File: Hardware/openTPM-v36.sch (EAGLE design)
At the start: 69 parts, among them U1 SAM4S4A, U2 TPS62172, U3 TC58CVG0S3HQAIEWSON, Y1 12MHZ, Y2 32KHz

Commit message: v36
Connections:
- new net N$19: U1.PA9/PGMM1, U3.CS
- new net N$24: U1.PA5/PGMRDY, U3.HOLD/SO3
- new net N$25: U1.PA6/PGMNOE, U3.WP/SO2
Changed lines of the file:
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@@
 <?xml version="1.0" encoding="utf-8"?>
 <!DOCTYPE eagle SYSTEM "eagle.dtd">
-<eagle version="8.1.1">
+<eagle version="7.4.0">
 <drawing>
 <settings>
@@
 <instance part="JP1" gate="G$1" x="45.72" y="116.84" rot="R180"/>
 <instance part="TPM1" gate="G$1" x="246.38" y="154.94"/>
-<instance part="GND1" gate="1" x="226.06" y="114.3"/>
-<instance part="GND2" gate="1" x="279.4" y="114.3"/>
+<instance part="GND1" gate="1" x="226.06" y="104.14"/>
+<instance part="GND2" gate="1" x="279.4" y="104.14"/>
 <instance part="GND3" gate="1" x="55.88" y="101.6"/>
 <instance part="GND5" gate="1" x="154.94" y="96.52"/>
@@
 <pinref part="GND2" gate="1" pin="GND"/>
 <wire x1="264.16" y1="142.24" x2="279.4" y2="142.24" width="0.1524" layer="91"/>
-<wire x1="279.4" y1="142.24" x2="279.4" y2="116.84" width="0.1524" layer="91"/>
+<wire x1="279.4" y1="142.24" x2="279.4" y2="106.68" width="0.1524" layer="91"/>
 <pinref part="TPM1" gate="G$1" pin="GND@25"/>
 <wire x1="264.16" y1="167.64" x2="279.4" y2="167.64" width="0.1524" layer="91"/>
@@
 <pinref part="TPM1" gate="G$1" pin="TESTBI"/>
 <wire x1="226.06" y1="134.62" x2="226.06" y2="132.08" width="0.1524" layer="91"/>
-<wire x1="226.06" y1="132.08" x2="226.06" y2="116.84" width="0.1524" layer="91"/>
+<wire x1="226.06" y1="132.08" x2="226.06" y2="106.68" width="0.1524" layer="91"/>
 <wire x1="231.14" y1="149.86" x2="226.06" y2="149.86" width="0.1524" layer="91"/>
 <wire x1="226.06" y1="149.86" x2="226.06" y2="142.24" width="0.1524" layer="91"/>
@@
 </segment>
 </net>
+<net name="N$19" class="0">
+<segment>
+<pinref part="U1" gate="G$1" pin="PA9/PGMM1"/>
+<wire x1="152.4" y1="149.86" x2="175.26" y2="149.86" width="0.1524" layer="91"/>
+<wire x1="175.26" y1="149.86" x2="175.26" y2="116.84" width="0.1524" layer="91"/>
+<wire x1="175.26" y1="116.84" x2="342.9" y2="116.84" width="0.1524" layer="91"/>
+<wire x1="342.9" y1="116.84" x2="342.9" y2="246.38" width="0.1524" layer="91"/>
+<pinref part="U3" gate="G$1" pin="CS"/>
+<wire x1="342.9" y1="246.38" x2="365.76" y2="246.38" width="0.1524" layer="91"/>
+</segment>
+</net>
+<net name="N$24" class="0">
+<segment>
+<pinref part="U1" gate="G$1" pin="PA5/PGMRDY"/>
+<wire x1="152.4" y1="160.02" x2="182.88" y2="160.02" width="0.1524" layer="91"/>
+<wire x1="182.88" y1="160.02" x2="182.88" y2="111.76" width="0.1524" layer="91"/>
+<wire x1="182.88" y1="111.76" x2="355.6" y2="111.76" width="0.1524" layer="91"/>
+<wire x1="355.6" y1="111.76" x2="355.6" y2="203.2" width="0.1524" layer="91"/>
+<wire x1="355.6" y1="203.2" x2="416.56" y2="203.2" width="0.1524" layer="91"/>
+<wire x1="416.56" y1="203.2" x2="416.56" y2="236.22" width="0.1524" layer="91"/>
+<pinref part="U3" gate="G$1" pin="HOLD/SO3"/>
+<wire x1="416.56" y1="236.22" x2="396.24" y2="236.22" width="0.1524" layer="91"/>
+</segment>
+</net>
+<net name="N$25" class="0">
+<segment>
+<pinref part="U1" gate="G$1" pin="PA6/PGMNOE"/>
+<wire x1="152.4" y1="157.48" x2="180.34" y2="157.48" width="0.1524" layer="91"/>
+<wire x1="180.34" y1="157.48" x2="180.34" y2="114.3" width="0.1524" layer="91"/>
+<wire x1="180.34" y1="114.3" x2="353.06" y2="114.3" width="0.1524" layer="91"/>
+<wire x1="353.06" y1="114.3" x2="353.06" y2="231.14" width="0.1524" layer="91"/>
+<pinref part="U3" gate="G$1" pin="WP/SO2"/>
+<wire x1="353.06" y1="231.14" x2="365.76" y2="231.14" width="0.1524" layer="91"/>
+</segment>
+</net>

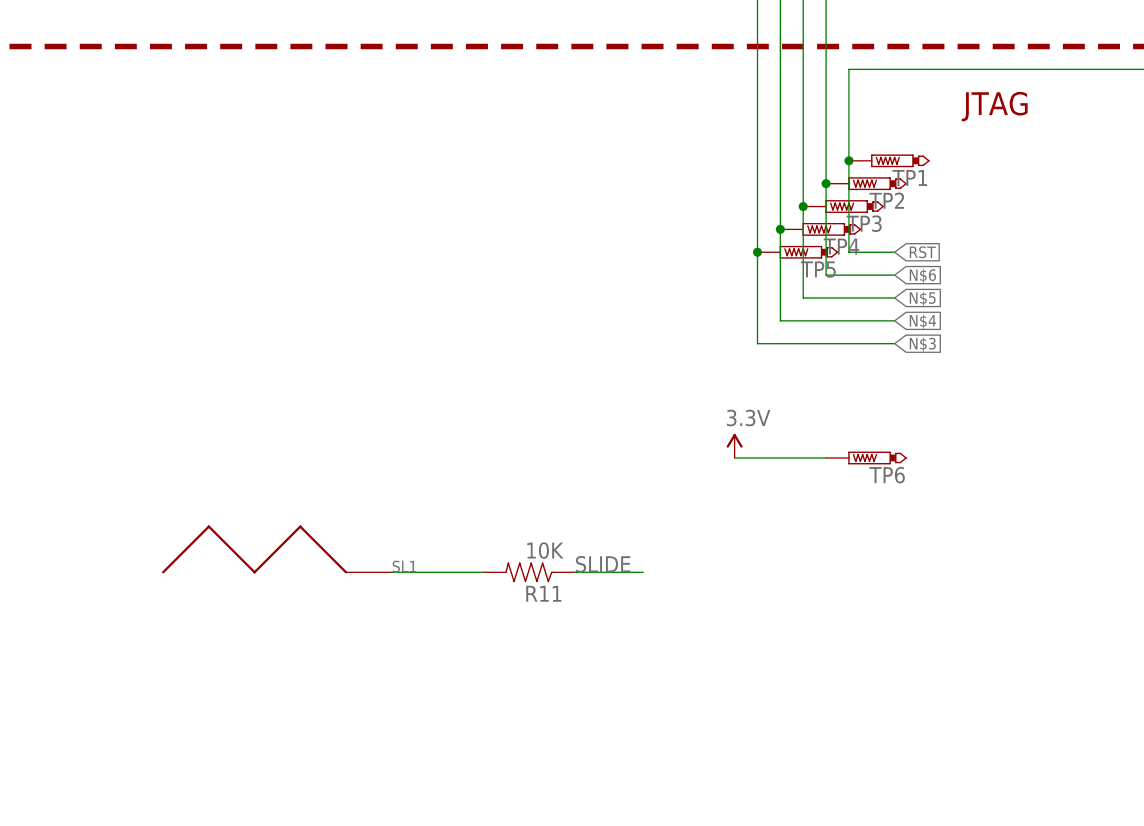
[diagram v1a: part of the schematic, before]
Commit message: cleaned silk up, added logo and binary words.
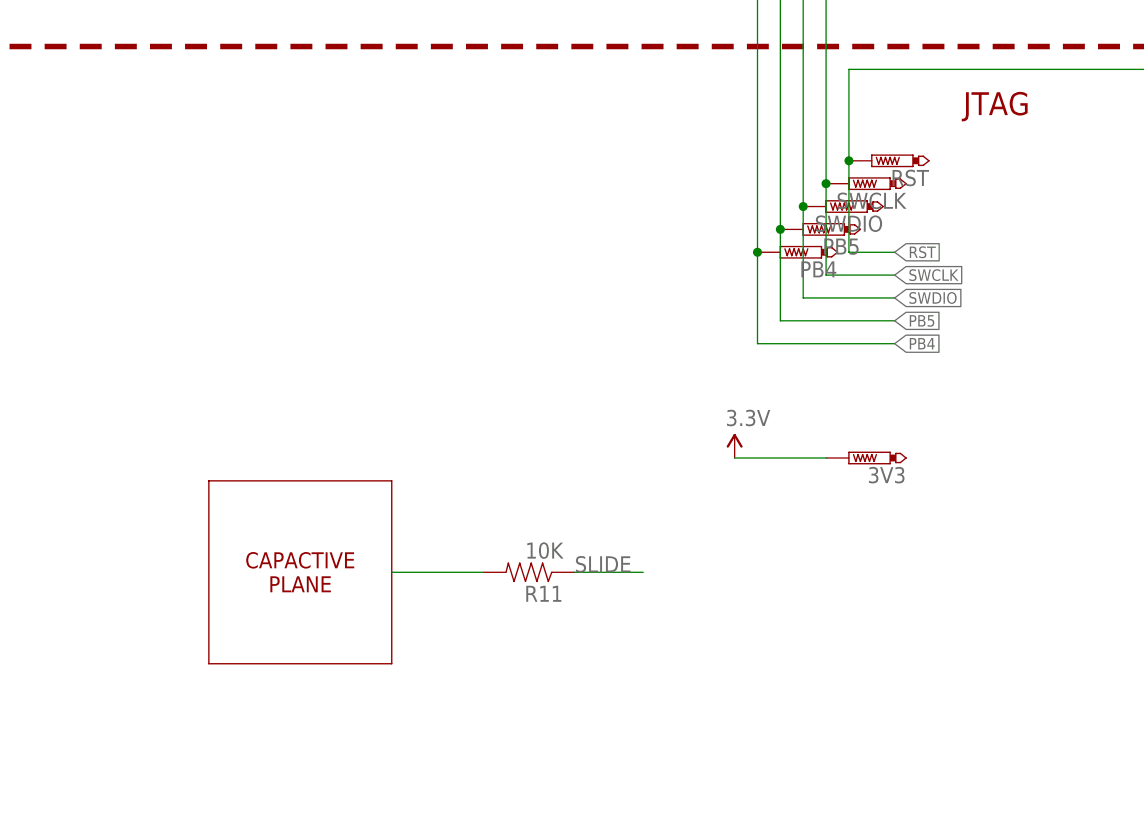
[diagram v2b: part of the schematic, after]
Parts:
- removed SL1: SLIDER_PASSIVE_1SEG, u2ftoken:SLIDER_PASSIVE_1SEG
- renumbered TP1 to RST, TP2 to SWCLK, TP3 to SWDIO, TP4 to PB5, TP5 to PB4, TP6 to 3V3
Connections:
- net N$3 renamed PB4
- net N$4 renamed PB5
- net N$5 renamed SWDIO
- net N$6 renamed SWCLK
- removed net N$7: R11.2, SL1.SL1
- new net CAP: R11.2
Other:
- note added: "CAPACTIVE PLANE"
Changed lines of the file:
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@@
 <?xml version="1.0" encoding="utf-8"?>
 <!DOCTYPE eagle SYSTEM "eagle.dtd">
-<eagle version="7.4.0">
+<eagle version="8.1.1">
 <drawing>
 <settings>
@@
 <part name="SUPPLY20" library="TPM" deviceset="3.3V" device=""/>
 <part name="GND23" library="TPM" deviceset="GND" device=""/>
-<part name="SL1" library="u2ftoken" deviceset="SLIDER_PASSIVE_1SEG" device=""/>
-<part name="TP1" library="CHEEPER-REV0.51A" deviceset="PTR1" device="B1,27"/>
-<part name="TP2" library="CHEEPER-REV0.51A" deviceset="PTR1" device="B1,27"/>
-<part name="TP3" library="CHEEPER-REV0.51A" deviceset="PTR1" device="B1,27"/>
-<part name="TP4" library="CHEEPER-REV0.51A" deviceset="PTR1" device="B1,27"/>
-<part name="TP5" library="CHEEPER-REV0.51A" deviceset="PTR1" device="B1,27"/>
+<part name="RST" library="CHEEPER-REV0.51A" deviceset="PTR1" device="B1,27"/>
+<part name="SWCLK" library="CHEEPER-REV0.51A" deviceset="PTR1" device="B1,27"/>
+<part name="SWDIO" library="CHEEPER-REV0.51A" deviceset="PTR1" device="B1,27"/>
+<part name="PB5" library="CHEEPER-REV0.51A" deviceset="PTR1" device="B1,27"/>
+<part name="PB4" library="CHEEPER-REV0.51A" deviceset="PTR1" device="B1,27"/>
 <part name="R11" library="TPM" deviceset="RESISTOR" device=".0402" value="10K"/>
-<part name="TP6" library="CHEEPER-REV0.51A" deviceset="PTR1" device="B1,27"/>
+<part name="3V3" library="CHEEPER-REV0.51A" deviceset="PTR1" device="B1,27"/>
 <part name="SUPPLY27" library="TPM" deviceset="3.3V" device=""/>
 </parts>
@@
 <text x="106.68" y="83.82" size="2.54" layer="94" font="vector" ratio="12">JTAG</text>
 <text x="363.22" y="187.96" size="2.54" layer="94" font="vector" ratio="12">Power Decoupling</text>
+<wire x1="43.18" y1="43.18" x2="22.86" y2="43.18" width="0.1524" layer="94"/>
+<wire x1="22.86" y1="43.18" x2="22.86" y2="22.86" width="0.1524" layer="94"/>
+<wire x1="22.86" y1="22.86" x2="43.18" y2="22.86" width="0.1524" layer="94"/>
+<wire x1="43.18" y1="22.86" x2="43.18" y2="43.18" width="0.1524" layer="94"/>
+<text x="33.02" y="33.02" size="1.778" layer="94" align="center">CAPACTIVE
+PLANE</text>
 </plain>
 <instances>
@@
 <instance part="SUPPLY20" gate="G$1" x="401.32" y="251.46"/>
 <instance part="GND23" gate="1" x="398.78" y="223.52"/>
-<instance part="SL1" gate="SL1" x="27.94" y="33.02"/>
-<instance part="TP1" gate="G$1" x="96.52" y="78.74" rot="R90"/>
-<instance part="TP2" gate="G$1" x="93.98" y="76.2" rot="R90"/>
-<instance part="TP3" gate="G$1" x="91.44" y="73.66" rot="R90"/>
-<instance part="TP4" gate="G$1" x="88.9" y="71.12" rot="R90"/>
-<instance part="TP5" gate="G$1" x="86.36" y="68.58" rot="R90"/>
+<instance part="RST" gate="G$1" x="96.52" y="78.74" rot="R90"/>
+<instance part="SWCLK" gate="G$1" x="93.98" y="76.2" rot="R90"/>
+<instance part="SWDIO" gate="G$1" x="91.44" y="73.66" rot="R90"/>
+<instance part="PB5" gate="G$1" x="88.9" y="71.12" rot="R90"/>
+<instance part="PB4" gate="G$1" x="86.36" y="68.58" rot="R90"/>
 <instance part="R11" gate="G$1" x="58.42" y="33.02" rot="R180"/>
-<instance part="TP6" gate="G$1" x="93.98" y="45.72" rot="R90"/>
+<instance part="3V3" gate="G$1" x="93.98" y="45.72" rot="R90"/>
 <instance part="SUPPLY27" gate="G$1" x="81.28" y="45.72"/>
 </instances>
@@
 </segment>
 </net>
-<net name="N$3" class="0">
+<net name="PB4" class="0">
 <segment>
 <pinref part="U1" gate="G$1" pin="TDI/PB4"/>
@@
 <wire x1="83.82" y1="58.42" x2="99.06" y2="58.42" width="0.1524" layer="91"/>
 <label x="99.06" y="58.42" size="1.27" layer="95" xref="yes"/>
-<pinref part="TP5" gate="G$1" pin="TP"/>
+<pinref part="PB4" gate="G$1" pin="TP"/>
 <junction x="83.82" y="68.58"/>
 </segment>
 </net>
-<net name="N$4" class="0">
+<net name="PB5" class="0">
 <segment>
 <pinref part="U1" gate="G$1" pin="TDO/TRACESWO/PB5"/>
@@
 <wire x1="86.36" y1="60.96" x2="99.06" y2="60.96" width="0.1524" layer="91"/>
 <label x="99.06" y="60.96" size="1.27" layer="95" xref="yes"/>
-<pinref part="TP4" gate="G$1" pin="TP"/>
+<pinref part="PB5" gate="G$1" pin="TP"/>
 <junction x="86.36" y="71.12"/>
 </segment>
 </net>
-<net name="N$5" class="0">
+<net name="SWDIO" class="0">
 <segment>
 <pinref part="U1" gate="G$1" pin="TMS/SWDIO/PB6"/>
@@
 <wire x1="88.9" y1="63.5" x2="99.06" y2="63.5" width="0.1524" layer="91"/>
 <label x="99.06" y="63.5" size="1.27" layer="95" xref="yes"/>
-<pinref part="TP3" gate="G$1" pin="TP"/>
+<pinref part="SWDIO" gate="G$1" pin="TP"/>
 <junction x="88.9" y="73.66"/>
 </segment>
 </net>
-<net name="N$6" class="0">
+<net name="SWCLK" class="0">
 <segment>
 <pinref part="U1" gate="G$1" pin="TCK/SWCLK/PB7"/>
@@
 <wire x1="91.44" y1="66.04" x2="99.06" y2="66.04" width="0.1524" layer="91"/>
 <label x="99.06" y="66.04" size="1.27" layer="95" xref="yes"/>
-<pinref part="TP2" gate="G$1" pin="TP"/>
+<pinref part="SWCLK" gate="G$1" pin="TP"/>
 <junction x="91.44" y="76.2"/>
 </segment>
@@
 </segment>
 <segment>
-<pinref part="TP6" gate="G$1" pin="TP"/>
+<pinref part="3V3" gate="G$1" pin="TP"/>
 <wire x1="91.44" y1="45.72" x2="81.28" y2="45.72" width="0.1524" layer="91"/>
 <pinref part="SUPPLY27" gate="G$1" pin="3.3V"/>
@@
 <wire x1="93.98" y1="68.58" x2="99.06" y2="68.58" width="0.1524" layer="91"/>
 <label x="99.06" y="68.58" size="1.27" layer="95" xref="yes"/>
-<pinref part="TP1" gate="G$1" pin="TP"/>
+<pinref part="RST" gate="G$1" pin="TP"/>
 <junction x="93.98" y="78.74"/>
 </segment>
@@
 </segment>
 </net>
-<net name="N$7" class="0">
-<segment>
-<pinref part="SL1" gate="SL1" pin="SL1"/>
+<net name="CAP" class="0">
+<segment>
 <wire x1="43.18" y1="33.02" x2="53.34" y2="33.02" width="0.1524" layer="91"/>
 <pinref part="R11" gate="G$1" pin="2"/>
@@
 </schematic>
 </drawing>
+<compatibility>
+<note version="6.3" minversion="6.2.2" severity="warning">
+Since Version 6.2.2 text objects can contain more than one line,
+which will not be processed correctly with this version.
+</note>
+</compatibility>
 </eagle>
